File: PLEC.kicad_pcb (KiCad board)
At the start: 4 copper layers, 80.3 x 83.8 mm, 101 parts, among them IC1 XBP9B-DMST-002, J1 Conn_01x02, J2 Conn_01x02, J3 Conn_01x06, J4 Conn_01x04, J5 Conn_01x03, K1 PB1167, K2 PB1167, K3 PB1167, K4 PB1167, Q1 KSC2073H2TU, U1 LM1085-5.0, U2 LM1085-3.3, U3 TLP222A-2, U4 TLP222A, U5 TLP222A-2, U6 HXS20, U7 NBPMANN150, U8 Teensy3.6

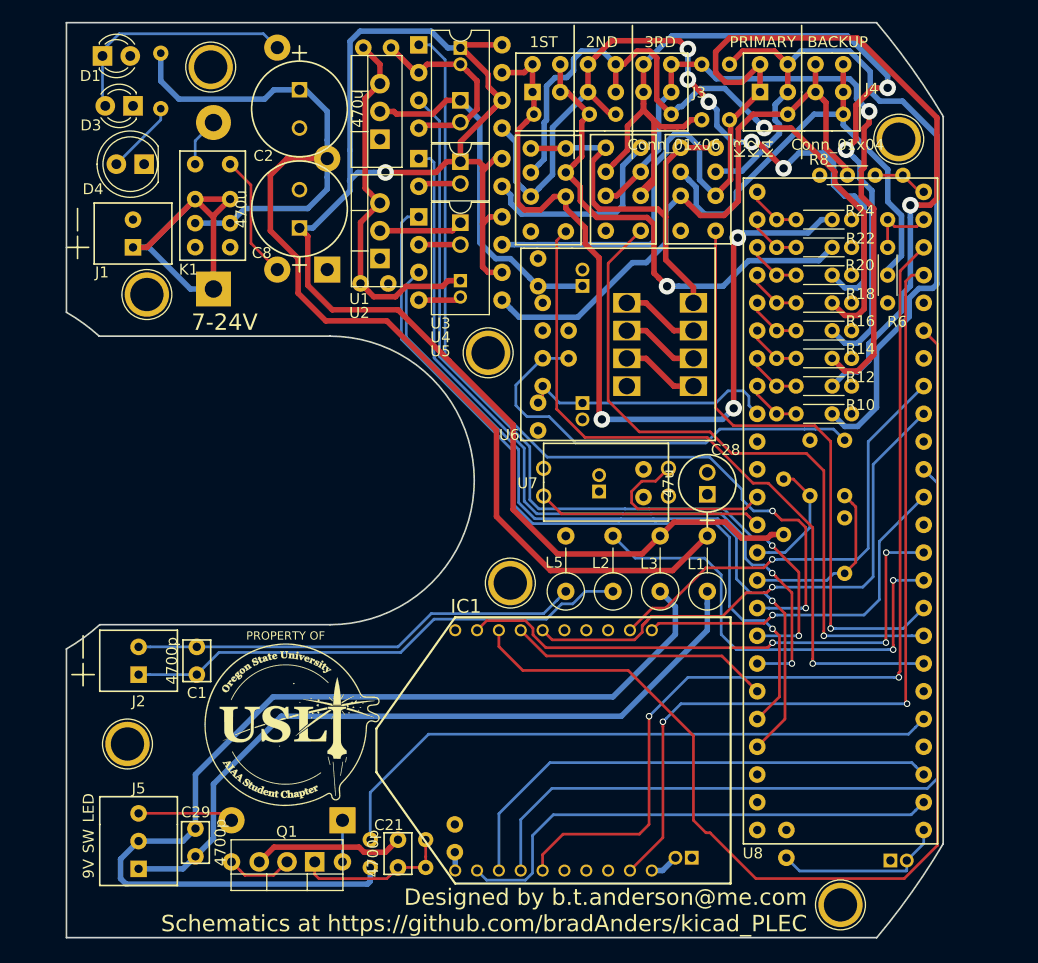
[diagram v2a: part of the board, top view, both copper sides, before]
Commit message: Replaced solid state relays with NPN Darlingtons
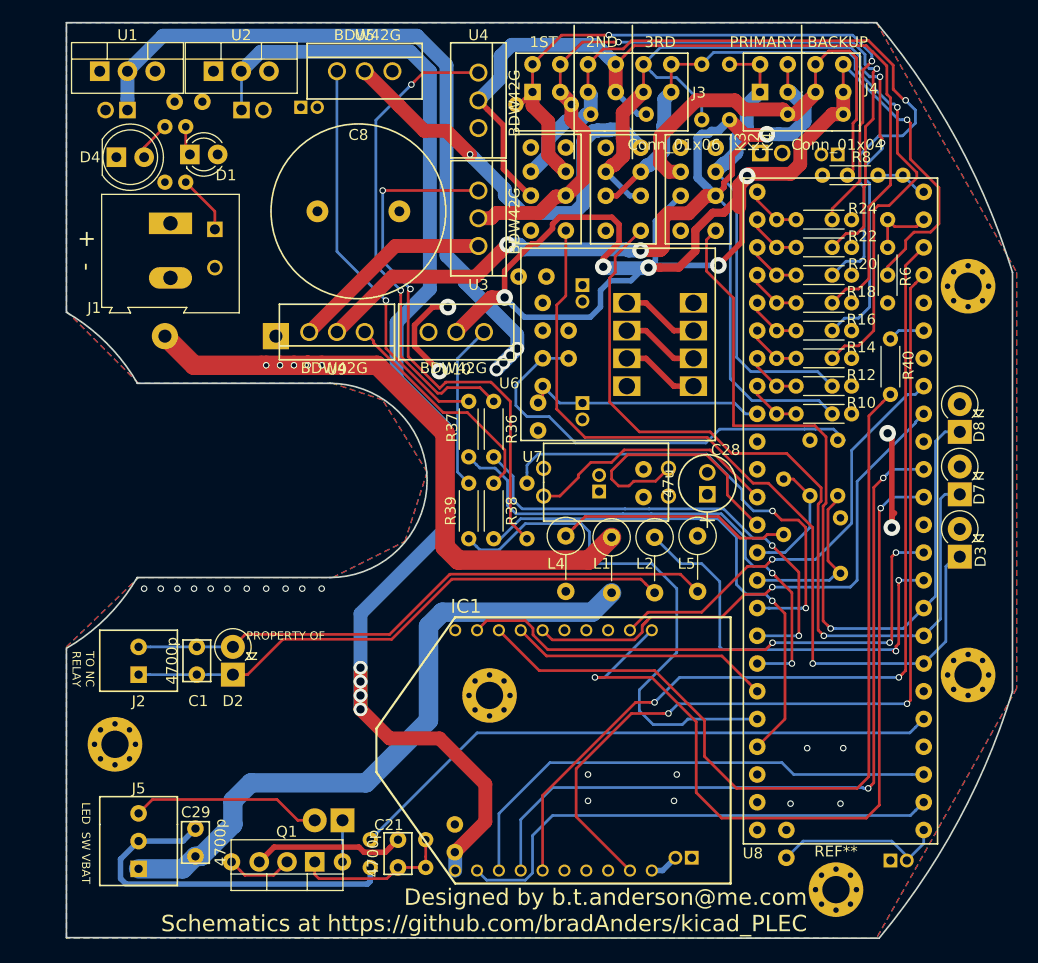
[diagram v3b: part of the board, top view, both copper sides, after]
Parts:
- removed C4: 1000p, PLEC:THTt_100Px200Lx125Wx200H_1000p
- removed G***: LOGO, PLEC:USLI_logo_820
- removed G***: LOGO, PLEC:USLI_logo_negative
- removed K1: PB1167, PLEC:PB1167
- removed L3: Ferrite_Bead_Small, Inductors_THT:L_Axial_L7.0mm_D3.3mm_P5.08mm_Vertical_Fastron_MICC
- removed the REF** at (110.2, 110.0)
- removed the REF** at (143.5, 136.4)
- removed the REF** at (141.5, 115.3)
- removed the REF** at (108.5, 151.1)
- removed the REF** at (173.7, 165.9)
- removed the REF** at (179.1, 95.8)
- removed the REF** at (116.1, 89.2)
- added D7: 1N4001, Diodes_THT:D_DO-41_SOD81_P2.54mm_Vertical_KathodeUp, F.Cu at (184.7, 128.3)
- added D8: 1N4001, Diodes_THT:D_DO-41_SOD81_P2.54mm_Vertical_KathodeUp, F.Cu at (184.7, 122.6)
- added L4: Ferrite_Bead_Small, Inductors_THT:L_Axial_L7.0mm_D3.3mm_P5.08mm_Vertical_Fastron_MICC, F.Cu at (148.6, 132.1)
- added R35: 150, Resistors_THT:R_Axial_DIN0204_L3.6mm_D1.6mm_P5.08mm_Horizontal, B.Cu at (145.0, 132.3)
- added R36: 150, Resistors_THT:R_Axial_DIN0204_L3.6mm_D1.6mm_P5.08mm_Horizontal, F.Cu at (142.0, 119.8)
- added R37: 150, Resistors_THT:R_Axial_DIN0204_L3.6mm_D1.6mm_P5.08mm_Horizontal, F.Cu at (139.7, 119.8)
- added R38: 150, Resistors_THT:R_Axial_DIN0204_L3.6mm_D1.6mm_P5.08mm_Horizontal, F.Cu at (142.0, 127.3)
- added R39: 150, Resistors_THT:R_Axial_DIN0204_L3.6mm_D1.6mm_P5.08mm_Horizontal, F.Cu at (139.7, 127.3)
- added R40: 33, Resistors_THT:R_Axial_DIN0204_L3.6mm_D1.6mm_P5.08mm_Horizontal, F.Cu at (178.3, 119.1)
- added REF**: MountingHole_2.5mm_Pad_Via, Mounting_Holes:MountingHole_2.5mm_Pad_Via, F.Cu at (173.3, 164.5)
- added REF**: MountingHole_2.5mm_Pad_Via, Mounting_Holes:MountingHole_2.5mm_Pad_Via, F.Cu at (141.6, 146.7)
- added REF**: MountingHole_2.5mm_Pad_Via, Mounting_Holes:MountingHole_2.5mm_Pad_Via, F.Cu at (107.3, 151.2)
- added REF**: MountingHole_2.5mm_Pad_Via, Mounting_Holes:MountingHole_2.5mm_Pad_Via, F.Cu at (185.4, 144.8)
- added REF**: MountingHole_2.5mm_Pad_Via, Mounting_Holes:MountingHole_2.5mm_Pad_Via, F.Cu at (185.4, 109.2)
- added U10: BDW42G, PLEC:BDW42G, F.Cu at (136.0, 113.4)
- added U9: BDW42G, PLEC:BDW42G, F.Cu at (125.1, 113.4)
- C2: moved to B.Cu
- C8: value 470u -> 5900u; footprint PLEC:THTm_5Px8Dx22H__470u -> PLEC:ELBK250
- D2: value D_Zener -> 1N4001; footprint Diodes_THT:D_DO-201AD_P15.24mm_Horizontal -> Diodes_THT:D_DO-41_SOD81_P2.54mm_Vertical_KathodeUp; moved to F.Cu
- D3: value LED_OL -> 1N4001; footprint LEDs:LED_D3.0mm_FlatTop -> Diodes_THT:D_DO-41_SOD81_P2.54mm_Vertical_KathodeUp
- D6: footprint Diodes_THT:D_DO-15_P10.16mm_Horizontal -> Diodes_THT:D_DO-41_SOD81_P2.54mm_Vertical_KathodeUp
- J1: footprint PLEC:THT_TerminalBlock_2.5mm_2pos -> Connectors_Terminal_Blocks:TerminalBlock_Altech_AK300-2_P5.00mm
- R25: value 600 -> 2k; footprint Resistors_THT:R_Axial_DIN0414_L11.9mm_D4.5mm_P20.32mm_Horizontal -> Resistors_THT:R_Axial_DIN0204_L3.6mm_D1.6mm_P5.08mm_Horizontal
- R32: value 100K -> 2K
- R33: value 100K -> 47K
- U3, U5: value TLP222A-2 -> BDW42G; footprint Housings_DIP:DIP-8_W7.62mm -> PLEC:BDW42G
- U4: value TLP222A -> BDW42G; footprint Housings_DIP:DIP-4_W7.62mm -> PLEC:BDW42G
- moved D3 86.2 mm to (184.7, 134.0), turned to 90 degrees
- moved D2 35.4 mm to (118.1, 144.8)
- moved C10 35.0 mm to (172.7, 97.2), turned to 180 degrees
- moved C6 31.5 mm to (107.5, 93.1), turned to 180 degrees
- moved C9 28.5 mm to (167.4, 97.0), turned to 0 degrees
- moved U1 26.4 mm to (105.9, 89.5), turned to 0 degrees
- moved C5 23.8 mm to (114.0, 92.3)
- moved U2 22.9 mm to (116.3, 89.5), turned to 0 degrees
- moved C7 22.2 mm to (119.9, 93.1), turned to 0 degrees
- moved C3 21.6 mm to (125.1, 92.8), turned to 0 degrees
- moved U3 19.2 mm to (140.6, 105.5), turned to 270 degrees
- moved C2 14.9 mm to (116.5, 105.7)
- moved U5 13.6 mm to (132.7, 89.5)
- moved L5 13.1 mm to (160.7, 132.1), turned to 270 degrees
- moved D1 12.1 mm to (114.2, 97.2)
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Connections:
- net ARMED_3V renamed /Microcontroller/A10
- net CURR_REF renamed /Current Sensor/Calibrate
- net CurrentData_2.5V renamed /Microcontroller/A11
- net EM_E1_VD+ renamed /Microcontroller/A6
- net EM_E1_VD- renamed /Microcontroller/A7
- net EM_E2_VD+ renamed /Microcontroller/A8
- net EM_E2_VD- renamed /Microcontroller/A9
- net EM_R1_VD+ renamed /Microcontroller/A0
- net EM_R1_VD- renamed /Microcontroller/A1
- net EM_R2_VD+ renamed /Microcontroller/A2
- net EM_R2_VD- renamed /Microcontroller/A3
- net EM_R3_VD+ renamed /Microcontroller/A4
- net EM_R3_VD- renamed /Microcontroller/A5
- net LED_CONTROL renamed /Microcontroller/D0
- net RLY_3_SHNT_SRC renamed /Microcontroller/D7
- net RLY_45_SHNT_SRC renamed /Microcontroller/D8
- net SPI_MISO renamed /Microcontroller/SPI_MISO
- net SPI_MOSI renamed /Microcontroller/SPI_MOSI
- net SPI_SS renamed /Microcontroller/SPI_SS
- net UART_TIXO renamed /Microcontroller/UART_RX
- net UART_TOXI renamed /RF Module/UART_RX
- net UART_~CTS renamed /Microcontroller/UART_~CTS
- net UART_~RTS renamed /Microcontroller/UART_~RTS
- net V_33 renamed /Power Rails/VCC_33
- net V_5 renamed /V_5
- net XB_~INTERRUPT renamed /Microcontroller/DATA_~INTERRUPT
- net XB_~RST renamed /Microcontroller/RF_~RESET
- net XB_~SLP renamed /Microcontroller/RF_~SLEEP
- C11 pad 1: EM_R1+ -> EM_R1-
- C11 pad 2: EM_R1- -> EM_R1+
- C12 pad 1: EM_R2+ -> EM_R2-
- C12 pad 2: EM_R2- -> EM_R2+
- C14 pad 1: EM_E1+ -> EM_E1-
- C14 pad 2: EM_E1- -> EM_E1+
- C15 pad 1: EM_E2+ -> EM_E2-
- C15 pad 2: EM_E2- -> EM_E2+
- C2 pad 1: V_9 -> /V_BAT
- C29 pad 2: /V9_Out -> /VBAT_OUT
- D2 pad 1: /V_Bat -> Net-(C1-Pad1)
- D2 pad 2: Net-(D2-Pad2) -> Net-(C1-Pad2)
- D3 pad 1: GND -> /Microcontroller/D6
- D3 pad 2: Net-(D1-Pad1) -> GND
- D5 pad 1: (no net) -> /Power Rails/V9_DIODE
- D5 pad 2: V_9 -> /V_BAT
- IC1 pad 13: (no net) -> Net-(IC1-Pad13)
- IC1 pad 15: (no net) -> Net-(IC1-Pad15)
- IC1 pad 18: SPI_CLK -> /RF Module/SPI_CLK
- IC1 pad 20: (no net) -> Net-(IC1-Pad20)
- IC1 pad 6: (no net) -> Net-(IC1-Pad6)
- IC1 pad 7: (no net) -> Net-(IC1-Pad7)
- IC1 pad 8: (no net) -> Net-(IC1-Pad8)
- J1 pad 1: /V_Bat -> /V_BAT
- J5 pad 1: /V9_Out -> /VBAT_OUT
- K2 pad 4: /Relays/R3D_SUPPLY -> Net-(K2-Pad4)
- K2 pad 5: /Current Sensor/CurrentIn -> SWITCH_RETURN
- K3 pad 1: RLY_12_SHNT_SRC -> /Microcontroller/D6
- K3 pad 2: EM_R1+ -> EM_R1-
- K3 pad 3: EM_R1- -> EM_R1+
- K3 pad 4: /Current Sensor/CurrentIn -> SWITCH_RETURN
- K3 pad 5: /Current Sensor/CurrentIn -> SWITCH_RETURN
- K3 pad 6: EM_R2- -> EM_R2+
- K3 pad 7: EM_R2+ -> EM_R2-
- K4 pad 2: EM_E1+ -> EM_E1-
- K4 pad 3: EM_E1- -> EM_E1+
- K4 pad 4: /Current Sensor/CurrentIn -> SWITCH_RETURN
- K4 pad 5: /Current Sensor/CurrentIn -> SWITCH_RETURN
- K4 pad 6: EM_E2- -> EM_E2+
- K4 pad 7: EM_E2+ -> EM_E2-
- L1 pad 1: /V9_Out -> /V_BAT
- L1 pad 2: V_9 -> /VBAT_OUT
- L2 pad 1: Net-(C1-Pad1) -> /Microcontroller/D9
- L2 pad 2: ROVER_RELAY -> Net-(C1-Pad1)
- L5 pad 1: Net-(C1-Pad2) -> GND
- L5 pad 2: GND -> Net-(C1-Pad2)
- R25 pad 1: Net-(K1-Pad8) -> /V_BAT
- R26 pad 1: V_9 -> /V_BAT
- R27 pad 1: EM_R1+ -> EM_R1-
- R27 pad 2: EM_R1- -> EM_R1+
- R28 pad 1: EM_R2+ -> EM_R2-
- R28 pad 2: EM_R2- -> EM_R2+
- R30 pad 1: EM_E1+ -> EM_E1-
- R30 pad 2: EM_E1- -> EM_E1+
- R31 pad 1: EM_E2+ -> EM_E2-
- R31 pad 2: EM_E2- -> EM_E2+
- U3 pad 1: RELAY_1_DRAIN -> Net-(R35-Pad1)
- U3 pad 2: GND -> EM_R1-
- U3 pad 3: RELAY_2_DRAIN -> /Current Sensor/CurrentIn
- U4 pad 1: RELAY_3_DRAIN -> Net-(R36-Pad1)
- U4 pad 2: GND -> EM_R2-
- U4 pad 3: /Relays/R3D_SUPPLY -> /Current Sensor/CurrentIn
- U5 pad 1: RELAY_4_DRAIN -> Net-(R37-Pad1)
- U5 pad 2: GND -> Net-(K2-Pad4)
- U5 pad 3: RELAY_5_DRAIN -> /Current Sensor/CurrentIn
- U7 pad 2: PRESSURE+ -> /Microcontroller/A13
- U7 pad 4: PRESSURE- -> /Microcontroller/A12
- U8 pad 10: ROVER_RELAY -> /Microcontroller/D9
- U8 pad 12: (no net) -> Net-(U8-Pad12)
- U8 pad 15: (no net) -> Net-(U8-Pad15)
- U8 pad 18: (no net) -> Net-(U8-Pad18)
- U8 pad 19: SPI_CLK -> /Microcontroller/SPI_CLK
- U8 pad 20: (no net) -> Net-(U8-Pad20)
- U8 pad 4: (no net) -> Net-(U8-Pad4)
- U8 pad 40: (no net) -> Net-(U8-Pad40)
- U8 pad 41: PRESSURE+ -> /Microcontroller/A12
- U8 pad 42: PRESSURE- -> /Microcontroller/A13
- U8 pad 45: RELAY_1_DRAIN -> /Microcontroller/D1
- U8 pad 46: RELAY_2_DRAIN -> /Microcontroller/D2
- U8 pad 47: RELAY_3_DRAIN -> /Microcontroller/D3
- U8 pad 49: RELAY_4_DRAIN -> /Microcontroller/D4
- U8 pad 50: RELAY_5_DRAIN -> /Microcontroller/D5
- U8 pad 51: (no net) -> Net-(U8-Pad51)
- U8 pad 52: (no net) -> Net-(U8-Pad52)
- U8 pad 6: (no net) -> Net-(U8-Pad6)
- U8 pad 7: RLY_12_SHNT_SRC -> /Microcontroller/D6
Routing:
- net SWITCH_RETURN: track 145.1 -> 21.6 mm, vias 1 -> 0
- net V_9: track 111.7 -> 0.00 mm
- net /Power Rails/VCC_33: track 9.37 -> 114.2 mm, vias 0 -> 4
- net SPI_CLK: track 103.9 -> 0.00 mm
- net EM_E2-: track 43.9 -> 129.5 mm, vias 0 -> 6
- net RELAY_1_DRAIN: track 81.9 -> 0.00 mm, vias 2 -> 0
- net /Microcontroller/D6: track 0.00 -> 78.5 mm, vias 0 -> 1
- net /RF Module/SPI_CLK: track 0.00 -> 78.1 mm
- net RELAY_2_DRAIN: track 77.8 -> 0.00 mm, vias 2 -> 0
- net RELAY_3_DRAIN: track 74.7 -> 0.00 mm, vias 2 -> 0
- net RELAY_4_DRAIN: track 73.4 -> 0.00 mm, vias 1 -> 0
- net RELAY_5_DRAIN: track 69.9 -> 0.00 mm, vias 1 -> 0
- net /V9_Out: track 67.6 -> 0.00 mm
- net RLY_12_SHNT_SRC: track 67.2 -> 0.00 mm, vias 1 -> 0
- net EM_E1+: track 107.5 -> 42.1 mm, vias 1 -> 0
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- added copper zone on In2.Cu, net /Current Sensor/CurrentIn
- added copper zone on In2.Cu, net /Power Rails/V9_DIODE
- added copper zone on In2.Cu, net /SW_IN
- added copper zone on In2.Cu, net /V_BAT
- added copper zone on B.Cu, net GND
- added copper zone on F.Cu, net GND
- removed copper zone on In2.Cu, net /V_Bat
- removed copper zone on In2.Cu, net V_9
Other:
- board size 80.3 x 83.8 mm -> 86.6 x 83.8 mm
- board text added: "+"
- board text added: "+ -"
- board text added: "LED"
- board text added: "SW"
- board text added: "TO NC RELAY"
- board text added: "VBAT"
- board text removed: "7-24V"

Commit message: Stiched vias and added mounting holes with no errors
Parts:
- removed REF** (x5): MountingHole_2.5mm_Pad_Via, Mounting_Holes:MountingHole_2.5mm_Pad_Via
- added G***: LOGO, PLEC:USLI_logo_820, B.Cu at (126.0, 127.0)
- added G***: LOGO, PLEC:USLI_logo_820, F.Cu at (102.9, 121.4)
- added J10: Conn_01x01, PLEC:Hole4-40, F.Cu at (90.4, 126.0)
- added J11: Conn_01x01, PLEC:Hole4-40, F.Cu at (160.8, 82.7)
- added J12: Conn_01x01, PLEC:Via-0.6mm, F.Cu at (151.6, 98.6)
- added J12: Conn_01x01, PLEC:Via-0.6mm, F.Cu at (150.0, 96.9)
- added J12: Conn_01x01, PLEC:Via-0.6mm, F.Cu at (149.1, 131.1)
- added J12: Conn_01x01, PLEC:Via-0.6mm, F.Cu at (144.1, 130.9)
- added J12: Conn_01x01, PLEC:Via-0.6mm, F.Cu at (146.9, 126.5)
- added J12: Conn_01x01, PLEC:Via-0.6mm, F.Cu at (131.1, 126.0)
- added J12: Conn_01x01, PLEC:Via-0.6mm, F.Cu at (126.5, 130.9)
- added J12: Conn_01x01, PLEC:Via-0.6mm, F.Cu at (133.2, 131.2)
- added J12: Conn_01x01, PLEC:Via-0.6mm, F.Cu at (133.2, 128.7)
- added J12: Conn_01x01, PLEC:Via-0.6mm, F.Cu at (126.5, 128.8)
- added J12: Conn_01x01, PLEC:Via-0.6mm, F.Cu at (118.1, 126.9)
- added J12: Conn_01x01, PLEC:Via-0.6mm, F.Cu at (109.5, 128.0)
- added J12: Conn_01x01, PLEC:Via-0.6mm, F.Cu at (122.7, 131.4)
- added J12: Conn_01x01, PLEC:Via-0.6mm, F.Cu at (104.4, 132.2)
- added J12: Conn_01x01, PLEC:Via-0.6mm, F.Cu at (100.3, 126.1)
- added J12: Conn_01x01, PLEC:Via-0.6mm, F.Cu at (84.3, 125.6)
- added J12: Conn_01x01, PLEC:Via-0.6mm, F.Cu at (99.3, 119.9)
- added J12: Conn_01x01, PLEC:Via-0.6mm, F.Cu at (95.0, 111.6)
- added J12: Conn_01x01, PLEC:Via-0.6mm, F.Cu at (89.8, 111.6)
- added J12: Conn_01x01, PLEC:Via-0.6mm, F.Cu at (85.0, 111.6)
- added J12: Conn_01x01, PLEC:Via-0.6mm, F.Cu at (81.9, 114.8)
- added J12: Conn_01x01, PLEC:Via-0.6mm, F.Cu at (100.3, 111.6)
- added J12: Conn_01x01, PLEC:Via-0.6mm, F.Cu at (104.5, 111.3)
- added J12: Conn_01x01, PLEC:Via-0.6mm, F.Cu at (122.0, 133.9)
- added J12: Conn_01x01, PLEC:Via-0.6mm, F.Cu at (110.1, 106.2)
- added J12: Conn_01x01, PLEC:Via-0.6mm, F.Cu at (110.6, 97.9)
- added J12: Conn_01x01, PLEC:Via-0.6mm, F.Cu at (105.3, 92.7)
- added J12: Conn_01x01, PLEC:Via-0.6mm, F.Cu at (86.7, 91.9)
- added J12: Conn_01x01, PLEC:Via-0.6mm, F.Cu at (84.7, 91.6)
- added J12: Conn_01x01, PLEC:Via-0.6mm, F.Cu at (82.0, 88.5)
- added J12: Conn_01x01, PLEC:Via-0.6mm, F.Cu at (78.6, 85.3)
- added J12: Conn_01x01, PLEC:Via-0.6mm, F.Cu at (78.6, 80.4)
- added J12: Conn_01x01, PLEC:Via-0.6mm, F.Cu at (78.6, 75.3)
- added J12: Conn_01x01, PLEC:Via-0.6mm, F.Cu at (78.6, 70.0)
- added J12: Conn_01x01, PLEC:Via-0.6mm, F.Cu at (120.0, 139.3)
- added J12: Conn_01x01, PLEC:Via-0.6mm, F.Cu at (78.6, 65.0)
- added J12: Conn_01x01, PLEC:Via-0.6mm, F.Cu at (78.6, 60.6)
- added J12: Conn_01x01, PLEC:Via-0.6mm, F.Cu at (84.1, 60.6)
- added J12: Conn_01x01, PLEC:Via-0.6mm, F.Cu at (111.4, 60.6)
- added J12: Conn_01x01, PLEC:Via-0.6mm, F.Cu at (115.4, 60.6)
- added J12: Conn_01x01, PLEC:Via-0.6mm, F.Cu at (121.3, 60.6)
- added J12: Conn_01x01, PLEC:Via-0.6mm, F.Cu at (129.9, 60.3)
- added J12: Conn_01x01, PLEC:Via-0.6mm, F.Cu at (136.5, 60.3)
- added J12: Conn_01x01, PLEC:Via-0.6mm, F.Cu at (141.1, 60.3)
- added J12: Conn_01x01, PLEC:Via-0.6mm, F.Cu at (146.2, 60.3)
- added J12: Conn_01x01, PLEC:Via-0.6mm, F.Cu at (117.6, 139.2)
- added J12: Conn_01x01, PLEC:Via-0.6mm, F.Cu at (151.0, 60.6)
- added J12: Conn_01x01, PLEC:Via-0.6mm, F.Cu at (154.2, 65.2)
- added J12: Conn_01x01, PLEC:Via-0.6mm, F.Cu at (158.1, 71.5)
- added J12: Conn_01x01, PLEC:Via-0.6mm, F.Cu at (160.7, 75.8)
- added J12: Conn_01x01, PLEC:Via-0.6mm, F.Cu at (162.1, 79.5)
- added J12: Conn_01x01, PLEC:Via-0.6mm, F.Cu at (163.3, 85.1)
- added J12: Conn_01x01, PLEC:Via-0.6mm, F.Cu at (163.3, 90.6)
- added J12: Conn_01x01, PLEC:Via-0.6mm, F.Cu at (163.3, 95.5)
- added J12: Conn_01x01, PLEC:Via-0.6mm, F.Cu at (163.3, 100.7)
- added J12: Conn_01x01, PLEC:Via-0.6mm, F.Cu at (163.3, 106.0)
- added J12: Conn_01x01, PLEC:Via-0.6mm, F.Cu at (115.3, 138.8)
- added J12: Conn_01x01, PLEC:Via-0.6mm, F.Cu at (163.3, 111.6)
- added J12: Conn_01x01, PLEC:Via-0.6mm, F.Cu at (163.3, 117.3)
- added J12: Conn_01x01, PLEC:Via-0.6mm, F.Cu at (161.9, 123.7)
- added J12: Conn_01x01, PLEC:Via-0.6mm, F.Cu at (160.1, 128.0)
- added J12: Conn_01x01, PLEC:Via-0.6mm, F.Cu at (158.5, 132.1)
- added J12: Conn_01x01, PLEC:Via-0.6mm, F.Cu at (156.3, 135.8)
- added J12: Conn_01x01, PLEC:Via-0.6mm, F.Cu at (153.8, 139.3)
- added J12: Conn_01x01, PLEC:Via-0.6mm, F.Cu at (151.5, 142.4)
- added J12: Conn_01x01, PLEC:Via-0.6mm, F.Cu at (144.5, 142.4)
- added J12: Conn_01x01, PLEC:Via-0.6mm, F.Cu at (139.2, 142.4)
- added J12: Conn_01x01, PLEC:Via-0.6mm, F.Cu at (123.4, 126.5)
- added J12: Conn_01x01, PLEC:Via-0.6mm, F.Cu at (133.0, 142.4)
- added J12: Conn_01x01, PLEC:Via-0.6mm, F.Cu at (126.4, 142.4)
- added J12: Conn_01x01, PLEC:Via-0.6mm, F.Cu at (120.5, 142.4)
- added J12: Conn_01x01, PLEC:Via-0.6mm, F.Cu at (114.7, 142.4)
- added J12: Conn_01x01, PLEC:Via-0.6mm, F.Cu at (109.3, 142.4)
- added J12: Conn_01x01, PLEC:Via-0.6mm, F.Cu at (103.6, 142.4)
- added J12: Conn_01x01, PLEC:Via-0.6mm, F.Cu at (97.9, 142.4)
- added J12: Conn_01x01, PLEC:Via-0.6mm, F.Cu at (92.3, 142.4)
- added J12: Conn_01x01, PLEC:Via-0.6mm, F.Cu at (86.5, 142.4)
- added J12: Conn_01x01, PLEC:Via-0.6mm, F.Cu at (81.2, 142.4)
- added J12: Conn_01x01, PLEC:Via-0.6mm, F.Cu at (121.3, 126.5)
- added J12: Conn_01x01, PLEC:Via-0.6mm, F.Cu at (78.5, 139.7)
- added J12: Conn_01x01, PLEC:Via-0.6mm, F.Cu at (78.6, 134.1)
- added J12: Conn_01x01, PLEC:Via-0.6mm, F.Cu at (78.6, 130.6)
- added J12: Conn_01x01, PLEC:Via-0.6mm, F.Cu at (78.6, 125.7)
- added J12: Conn_01x01, PLEC:Via-0.6mm, F.Cu at (78.6, 121.4)
- added J12: Conn_01x01, PLEC:Via-0.6mm, F.Cu at (78.6, 117.9)
- added J12: Conn_01x01, PLEC:Via-0.6mm, F.Cu at (122.0, 128.1)
- added J12: Conn_01x01, PLEC:Via-0.6mm, F.Cu at (120.9, 129.4)
- added J12: Conn_01x01, PLEC:Via-0.6mm, F.Cu at (153.4, 95.8)
- added J12: Conn_01x01, PLEC:Via-0.6mm, F.Cu at (119.1, 131.1)
- added J12: Conn_01x01, PLEC:Via-0.6mm, F.Cu at (117.2, 135.6)
- added J12: Conn_01x01, PLEC:Via-0.6mm, F.Cu at (117.2, 133.9)
- added J12: Conn_01x01, PLEC:Via-0.6mm, F.Cu at (117.2, 132.3)
- added J12: Conn_01x01, PLEC:Via-0.6mm, F.Cu at (119.9, 128.0)
- added J12: Conn_01x01, PLEC:Via-0.6mm, F.Cu at (118.5, 129.4)
- added J12: Conn_01x01, PLEC:Via-0.6mm, F.Cu at (117.2, 130.7)
- added J12: Conn_01x01, PLEC:Via-0.6mm, F.Cu at (153.2, 131.3)
- added J12: Conn_01x01, PLEC:Via-0.6mm, F.Cu at (153.3, 129.2)
- added J12: Conn_01x01, PLEC:Via-0.6mm, F.Cu at (145.4, 127.4)
- added J12: Conn_01x01, PLEC:Via-0.6mm, F.Cu at (150.6, 95.2)
- added J12: Conn_01x01, PLEC:Via-0.6mm, F.Cu at (133.3, 105.9)
- added J12: Conn_01x01, PLEC:Via-0.6mm, F.Cu at (129.3, 107.8)
- added J12: Conn_01x01, PLEC:Via-0.6mm, F.Cu at (137.5, 109.1)
- added J12: Conn_01x01, PLEC:Via-0.6mm, F.Cu at (129.4, 112.5)
- added J12: Conn_01x01, PLEC:Via-0.6mm, F.Cu at (114.0, 111.9)
- added J12: Conn_01x01, PLEC:Via-0.6mm, F.Cu at (120.4, 111.9)
- added J12: Conn_01x01, PLEC:Via-0.6mm, F.Cu at (118.5, 111.9)
- added J12: Conn_01x01, PLEC:Via-0.6mm, F.Cu at (137.5, 126.0)
- added J12: Conn_01x01, PLEC:Via-0.6mm, F.Cu at (137.5, 130.8)
- added J12: Conn_01x01, PLEC:Via-0.6mm, F.Cu at (136.3, 128.7)
- added J12: Conn_01x01, PLEC:Via-0.6mm, F.Cu at (151.4, 94.2)
- added J12: Conn_01x01, PLEC:Via-0.6mm, F.Cu at (134.0, 126.0)
- added J12: Conn_01x01, PLEC:Via-0.6mm, F.Cu at (134.2, 120.8)
- added J12: Conn_01x01, PLEC:Via-0.6mm, F.Cu at (132.8, 119.1)
- added J12: Conn_01x01, PLEC:Via-0.6mm, F.Cu at (128.5, 120.5)
- added J12: Conn_01x01, PLEC:Via-0.6mm, F.Cu at (123.1, 119.8)
- added J12: Conn_01x01, PLEC:Via-0.6mm, F.Cu at (119.3, 119.1)
- added J12: Conn_01x01, PLEC:Via-0.6mm, F.Cu at (117.5, 116.8)
- added J12: Conn_01x01, PLEC:Via-0.6mm, F.Cu at (121.0, 118.2)
- added J12: Conn_01x01, PLEC:Via-0.6mm, F.Cu at (123.2, 118.4)
- added J12: Conn_01x01, PLEC:Via-0.6mm, F.Cu at (126.2, 118.4)
- added J12: Conn_01x01, PLEC:Via-0.6mm, F.Cu at (150.0, 99.1)
- added J12: Conn_01x01, PLEC:Via-0.6mm, F.Cu at (127.9, 126.4)
- added J12: Conn_01x01, PLEC:Via-0.6mm, F.Cu at (131.6, 133.6)
- added J12: Conn_01x01, PLEC:Via-0.6mm, F.Cu at (126.5, 133.2)
- added J12: Conn_01x01, PLEC:Via-0.6mm, F.Cu at (129.9, 131.1)
- added J12: Conn_01x01, PLEC:Via-0.6mm, F.Cu at (129.9, 128.7)
- added J12: Conn_01x01, PLEC:Via-0.6mm, F.Cu at (145.7, 133.2)
- added J12: Conn_01x01, PLEC:Via-0.6mm, F.Cu at (147.8, 133.3)
- added J12: Conn_01x01, PLEC:Via-0.6mm, F.Cu at (150.0, 133.5)
- added J12: Conn_01x01, PLEC:Via-0.6mm, F.Cu at (146.8, 130.9)
- added J12: Conn_01x01, PLEC:Via-0.6mm, F.Cu at (142.5, 130.9)
- added J12: Conn_01x01, PLEC:Via-0.6mm, F.Cu at (150.1, 101.2)
- added J12: Conn_01x01, PLEC:Via-0.6mm, F.Cu at (142.5, 129.0)
- added J12: Conn_01x01, PLEC:Via-0.6mm, F.Cu at (144.5, 129.0)
- added J12: Conn_01x01, PLEC:Via-0.6mm, F.Cu at (146.8, 129.0)
- added J12: Conn_01x01, PLEC:Via-0.6mm, F.Cu at (149.0, 129.0)
- added J12: Conn_01x01, PLEC:Via-0.6mm, F.Cu at (151.0, 130.8)
- added J12: Conn_01x01, PLEC:Via-0.6mm, F.Cu at (150.1, 112.1)
- added J12: Conn_01x01, PLEC:Via-0.6mm, F.Cu at (150.1, 114.0)
- added J12: Conn_01x01, PLEC:Via-0.6mm, F.Cu at (152.7, 120.8)
- added J12: Conn_01x01, PLEC:Via-0.6mm, F.Cu at (150.1, 120.8)
- added J12: Conn_01x01, PLEC:Via-0.6mm, F.Cu at (150.1, 123.3)
- added J12: Conn_01x01, PLEC:Via-0.6mm, F.Cu at (150.1, 103.8)
- added J12: Conn_01x01, PLEC:Via-0.6mm, F.Cu at (152.7, 123.3)
- added J12: Conn_01x01, PLEC:Via-0.6mm, F.Cu at (152.7, 125.6)
- added J12: Conn_01x01, PLEC:Via-0.6mm, F.Cu at (152.7, 127.6)
- added J12: Conn_01x01, PLEC:Via-0.6mm, F.Cu at (150.1, 125.6)
- added J12: Conn_01x01, PLEC:Via-0.6mm, F.Cu at (150.1, 127.6)
- added J12: Conn_01x01, PLEC:Via-0.6mm, F.Cu at (159.8, 113.7)
- added J12: Conn_01x01, PLEC:Via-0.6mm, F.Cu at (159.3, 89.5)
- added J12: Conn_01x01, PLEC:Via-0.6mm, F.Cu at (154.4, 76.5)
- added J12: Conn_01x01, PLEC:Via-0.6mm, F.Cu at (143.8, 75.6)
- added J12: Conn_01x01, PLEC:Via-0.6mm, F.Cu at (132.5, 84.1)
- added J12: Conn_01x01, PLEC:Via-0.6mm, F.Cu at (150.1, 106.6)
- added J12: Conn_01x01, PLEC:Via-0.6mm, F.Cu at (100.2, 67.8)
- added J12: Conn_01x01, PLEC:Via-0.6mm, F.Cu at (104.1, 79.2)
- added J12: Conn_01x01, PLEC:Via-0.6mm, F.Cu at (104.0, 71.5)
- added J12: Conn_01x01, PLEC:Via-0.6mm, F.Cu at (94.6, 74.4)
- added J12: Conn_01x01, PLEC:Via-0.6mm, F.Cu at (96.4, 83.7)
- added J12: Conn_01x01, PLEC:Via-0.6mm, F.Cu at (83.3, 80.1)
- added J12: Conn_01x01, PLEC:Via-0.6mm, F.Cu at (116.6, 111.9)
- added J12: Conn_01x01, PLEC:Via-0.6mm, F.Cu at (121.3, 107.2)
- added J12: Conn_01x01, PLEC:Via-0.6mm, F.Cu at (109.1, 111.5)
- added J12: Conn_01x01, PLEC:Via-0.6mm, F.Cu at (139.6, 137.5)
- added J12: Conn_01x01, PLEC:Via-0.6mm, F.Cu at (150.1, 109.1)
- added J12: Conn_01x01, PLEC:Via-0.6mm, F.Cu at (129.3, 134.1)
- added J12: Conn_01x01, PLEC:Via-0.6mm, F.Cu at (123.1, 135.1)
- added J12: Conn_01x01, PLEC:Via-0.6mm, F.Cu at (127.5, 96.5)
- added J12: Conn_01x01, PLEC:Via-0.6mm, F.Cu at (135.4, 95.6)
- added J12: Conn_01x01, PLEC:Via-0.6mm, F.Cu at (145.9, 95.5)
- added J12: Conn_01x01, PLEC:Via-0.6mm, F.Cu at (145.9, 93.0)
- added J12: Conn_01x01, PLEC:Via-0.6mm, F.Cu at (119.6, 103.4)
- added J12: Conn_01x01, PLEC:Via-0.6mm, F.Cu at (148.3, 108.0)
- added J12: Conn_01x01, PLEC:Via-0.6mm, F.Cu at (137.2, 124.1)
- added J12: Conn_01x01, PLEC:Via-0.6mm, F.Cu at (137.2, 122.7)
- added J6: Conn_01x01, PLEC:Hole4-40, F.Cu at (95.2, 69.3)
- added J7: Conn_01x01, PLEC:Hole4-40, F.Cu at (148.5, 139.6)
- added J8: Conn_01x01, PLEC:Hole4-40, F.Cu at (115.8, 120.0)
- added J9: Conn_01x01, PLEC:Hole4-40, F.Cu at (160.8, 120.8)
- C29: moved to B.Cu
- J5: footprint PLEC:THT_TerminalBlock_2.5mm_3pos -> Connectors_Terminal_Blocks:TerminalBlock_bornier-3_P5.08mm
- moved C29 40.6 mm to (86.4, 131.1), turned to 0 degrees
- moved D6 38.5 mm to (99.8, 132.1)
- moved C3 38.2 mm to (99.2, 64.7), turned to 270 degrees
- moved R34 35.9 mm to (93.5, 135.6)
- moved C21 35.9 mm to (107.8, 135.8)
- moved C11 35.9 mm to (121.4, 63.5)
- moved C13 35.9 mm to (131.6, 63.5)
- moved C15 35.9 mm to (147.3, 63.5)
- moved C16 35.9 mm to (124.7, 95.2)
- moved C17 35.9 mm to (120.7, 95.8)
- moved C18 35.9 mm to (124.7, 84.5)
- moved C19 35.9 mm to (120.1, 82.9)
- moved C2 35.9 mm to (91.1, 80.3)
- moved C25 35.9 mm to (130.3, 101.9)
- moved C27 35.9 mm to (153.6, 136.4)
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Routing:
- net /SW_IN: track 34.2 -> 23.3 mm
- net /LED_CATHODE: track 17.4 -> 23.5 mm
- net /VBAT_OUT: track 60.1 -> 57.7 mm
- net /Power Rails/VCC_33: track 114.2 -> 111.8 mm
- net Net-(D6-Pad1): track 3.81 -> 5.28 mm
- net Net-(C21-Pad1): track 14.4 -> 13.0 mm
- net GND: track 120.9 -> 120.0 mm, vias 23 -> 4
- added copper zone on In2.Cu, net GND
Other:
- outline, holes or cut-outs redrawn
